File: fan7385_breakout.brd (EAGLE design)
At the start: 28.6 x 15.2 mm, 17 parts

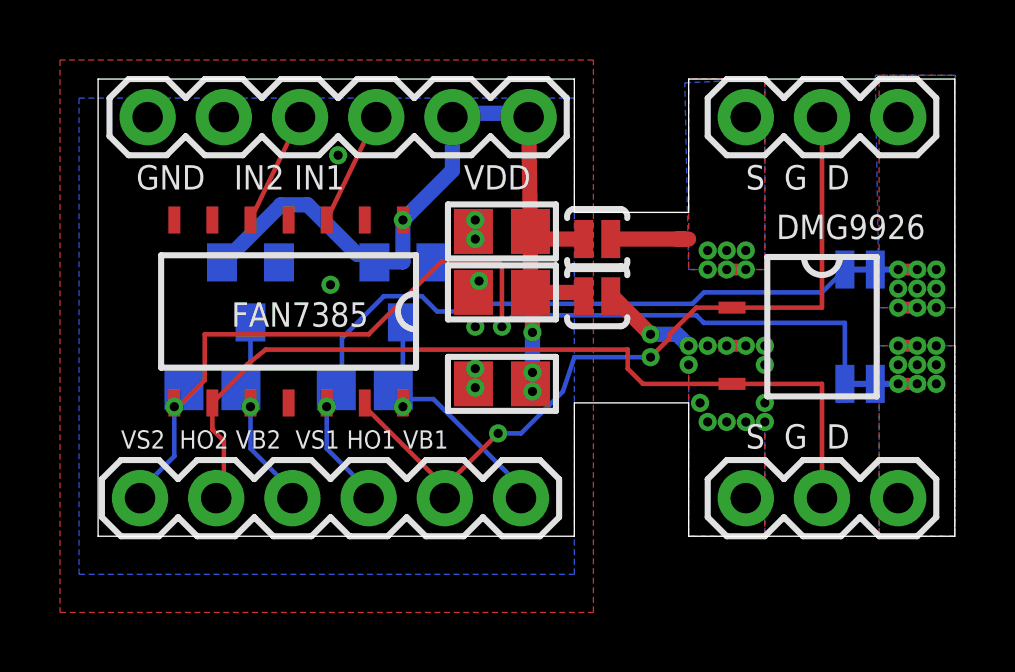
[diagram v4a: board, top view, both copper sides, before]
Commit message: UAAH! mixed source and drain for the cboot return...
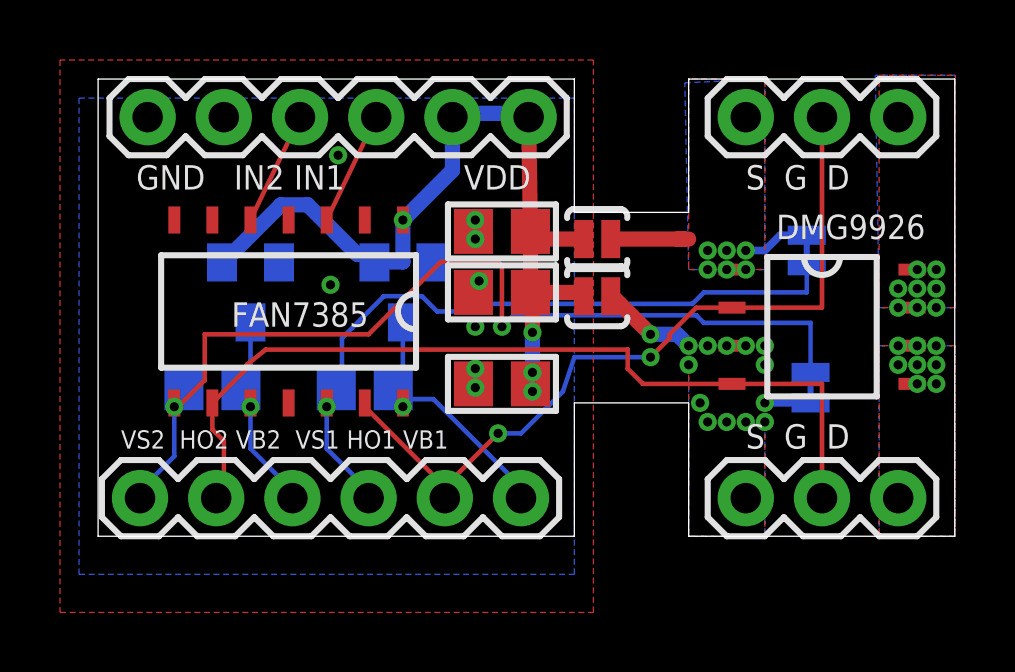
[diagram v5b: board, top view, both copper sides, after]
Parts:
- moved SJ3 1.89 mm to (23.6, 9.53), turned to 90 degrees
- moved SJ4 1.66 mm to (23.7, 4.95), turned to 270 degrees
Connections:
- net D1: no longer SJ3.2
- net D2: no longer SJ4.2
- net S1: now also SJ3.2
- net S2: now also SJ4.2
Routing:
- net S1: track 2.60 -> 4.84 mm
- net VS2: track 34.3 -> 32.8 mm
- net S2: track 3.46 -> 4.99 mm
- net D2: track 0.76 -> 0.00 mm, vias 9 -> 8
- net D1: track 0.76 -> 0.00 mm, vias 9 -> 8
- net VS1: track 24.7 -> 24.0 mm
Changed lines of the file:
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@@
 <element name="SJ1" library="SparkFun-Passives" package="SJ_2S-NO" value="SOLDERJUMPERNO" x="16.637" y="8.001" smashed="yes"/>
 <element name="SJ2" library="SparkFun-Passives" package="SJ_2S-NO" value="SOLDERJUMPERNO" x="16.637" y="9.906" smashed="yes"/>
-<element name="SJ3" library="SparkFun-Passives" package="SJ_2S-TRACE" value="SOLDERJUMPERTRACE" x="25.4" y="8.89" smashed="yes" rot="MR180"/>
-<element name="SJ4" library="SparkFun-Passives" package="SJ_2S-TRACE" value="SOLDERJUMPERTRACE" x="25.4" y="5.08" smashed="yes" rot="MR180"/>
+<element name="SJ3" library="SparkFun-Passives" package="SJ_2S-TRACE" value="SOLDERJUMPERTRACE" x="23.622" y="9.525" smashed="yes" rot="MR90"/>
+<element name="SJ4" library="SparkFun-Passives" package="SJ_2S-TRACE" value="SOLDERJUMPERTRACE" x="23.749" y="4.953" smashed="yes" rot="MR270"/>
 <element name="JP1" library="SparkFun-Connectors" package="1X06" value="" x="1.651" y="13.97" smashed="yes">
 <attribute name="VALUE" x="0.381" y="10.795" size="1.27" layer="27"/>
@@
 <wire x1="17.145" y1="9.906" x2="17.087" y2="9.906" width="0.508" layer="1"/>
 <wire x1="19.304" y1="9.906" x2="19.431" y2="9.906" width="0.508" layer="1"/>
+<contactref element="SJ3" pad="2"/>
+<wire x1="21.59" y1="9.525" x2="22.225" y2="9.525" width="0.254" layer="16"/>
+<wire x1="22.225" y1="9.525" x2="22.733" y2="10.033" width="0.254" layer="16"/>
+<wire x1="22.733" y1="10.033" x2="23.622" y2="10.033" width="0.254" layer="16"/>
 </signal>
 <signal name="S2" class="2">
@@
 <via x="21.59" y="3.81" extent="1-16" drill="0.3048" shape="square"/>
 <via x="22.225" y="3.81" extent="1-16" drill="0.3048" shape="square"/>
+<contactref element="SJ4" pad="2"/>
+<wire x1="22.225" y1="4.445" x2="23.749" y2="4.445" width="0.254" layer="16"/>
 </signal>
 <signal name="IN1">
@@
 <via x="27.305" y="6.35" extent="1-16" drill="0.3048" shape="square"/>
 <via x="27.305" y="5.08" extent="1-16" drill="0.3048" shape="square"/>
-<via x="26.67" y="5.08" extent="1-16" drill="0.3048" shape="square"/>
 <via x="26.67" y="5.715" extent="1-16" drill="0.3048" shape="square"/>
 <via x="27.94" y="5.715" extent="1-16" drill="0.3048" shape="square"/>
@@
 <via x="27.94" y="6.35" extent="1-16" drill="0.3048" shape="square"/>
 <via x="26.67" y="6.35" extent="1-16" drill="0.3048" shape="square"/>
-<contactref element="SJ4" pad="2"/>
 <contactref element="JP3" pad="3"/>
-<wire x1="26.67" y1="5.08" x2="25.908" y2="5.08" width="0.2032" layer="16"/>
 </signal>
 <signal name="D1" class="2">
@@
 <via x="26.67" y="7.62" extent="1-16" drill="0.3048" shape="square"/>
 <via x="27.305" y="7.62" extent="1-16" drill="0.3048" shape="square"/>
-<via x="26.67" y="8.89" extent="1-16" drill="0.3048" shape="square"/>
 <via x="27.305" y="8.89" extent="1-16" drill="0.3048" shape="square"/>
 <via x="27.94" y="8.89" extent="1-16" drill="0.3048" shape="square"/>
-<contactref element="SJ3" pad="2"/>
 <contactref element="JP4" pad="3"/>
-<wire x1="26.67" y1="8.89" x2="25.908" y2="8.89" width="0.2032" layer="16"/>
 </signal>
 <signal name="VS1">
@@
 <contactref element="JP2" pad="4"/>
 <via x="7.62" y="4.318" extent="1-16" drill="0.3048" shape="square"/>
-<wire x1="24.892" y1="8.89" x2="24.13" y2="8.128" width="0.1524" layer="16"/>
-<wire x1="24.13" y1="8.128" x2="20.193" y2="8.128" width="0.1524" layer="16"/>
+<wire x1="23.622" y1="9.017" x2="23.622" y2="8.128" width="0.1524" layer="16"/>
+<wire x1="23.622" y1="8.128" x2="20.193" y2="8.128" width="0.1524" layer="16"/>
 <wire x1="7.62" y1="4.318" x2="7.62" y2="4.443" width="0.1524" layer="1"/>
 <wire x1="7.62" y1="4.953" x2="7.62" y2="4.318" width="0.1524" layer="16"/>
@@
 <contactref element="JP2" pad="1"/>
 <via x="2.54" y="4.318" extent="1-16" drill="0.3048" shape="square"/>
-<wire x1="24.892" y1="5.08" x2="24.892" y2="7.112" width="0.1524" layer="16"/>
-<wire x1="24.892" y1="7.112" x2="20.193" y2="7.112" width="0.1524" layer="16"/>
+<wire x1="23.749" y1="5.461" x2="23.749" y2="7.112" width="0.1524" layer="16"/>
+<wire x1="23.749" y1="7.112" x2="20.193" y2="7.112" width="0.1524" layer="16"/>
 <wire x1="2.54" y1="4.318" x2="2.54" y2="4.443" width="0.1524" layer="1"/>
 <wire x1="2.54" y1="4.953" x2="2.54" y2="4.318" width="0.1524" layer="16"/>
@@
 </signal>
 </signals>
-<errors>
-</errors>
 </board>
 </drawing>
